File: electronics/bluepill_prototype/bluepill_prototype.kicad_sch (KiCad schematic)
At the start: 8 parts, among them M1 Motor_DC, SW1 SW_SPST, U1 Open_drain_hall_sensor, U2 YAAJ_BluePill_Part_Like

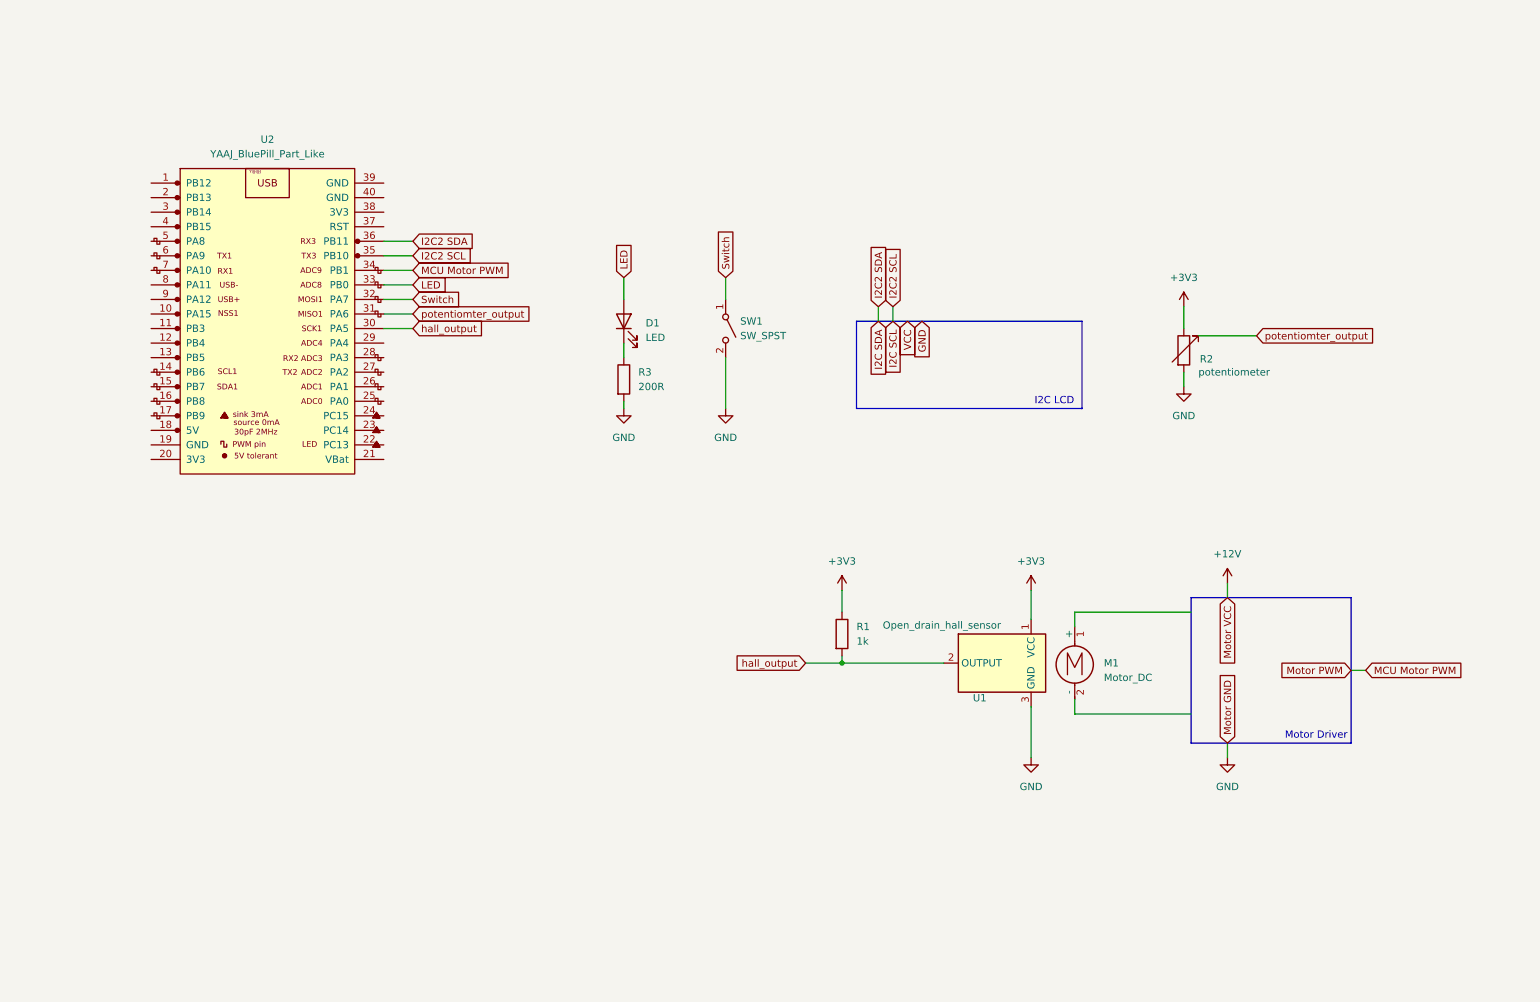
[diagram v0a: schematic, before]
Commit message: feat: updated electronic schematic
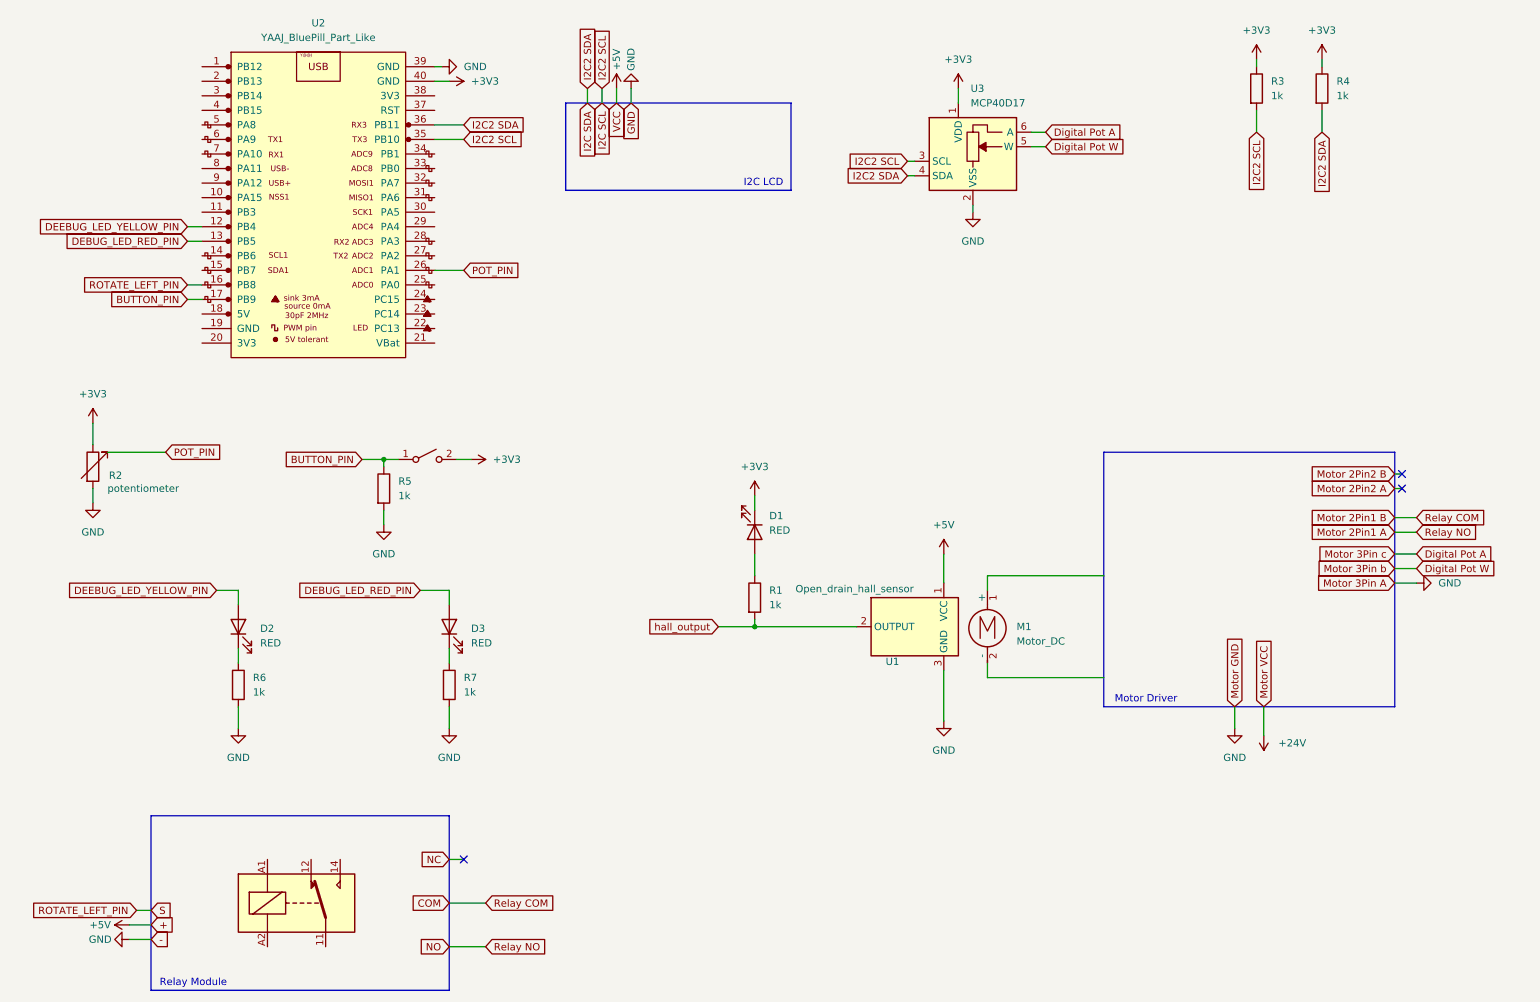
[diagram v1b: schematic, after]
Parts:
- added D2, D3: RED, symbol Device:LED
- added K1: Fujitsu_FTR-LYCA005x, Relay_THT:Relay_SPDT_Fujitsu_FTR-LYCA005x_FormC_Vertical, symbol Relay:Fujitsu_FTR-LYCA005x
- added R4, R5, R6, R7: 1k, symbol Device:R
- added U3: MCP40D17, Package_TO_SOT_SMD:SOT-363_SC-70-6, symbol Potentiometer_Digital:MCP4018-xxxxLT
- D1: value LED -> RED
- R3: value 200R -> 1k
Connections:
- net +3V3: now also D1.1 (K), R3.1, SW1.2 (B), U2.40 (GND), R4.1, U3.1 (VDD); no longer R1.1, U1.1 (VCC)
- net GND: now also U2.39 (GND), R5.2, R6.2, R7.2, U3.2 (VSS); no longer R3.2, SW1.2 (B)
- net I2C SCL: now also R3.2, U3.3 (SCL)
- net I2C SDA: now also R4.2, U3.4 (SDA)
- net hall_output: no longer U2.30 (PA5)
- net DEEBUG_LED_YELLOW_PIN: now reaches U2.12 (PB4)
- net DEEBUG_LED_YELLOW_PIN: now also D2.2 (A)
- net DEBUG_LED_RED_PIN: now reaches U2.13 (PB5)
- net DEBUG_LED_RED_PIN: now also D3.2 (A)
- net ROTATE_LEFT_PIN: now reaches U2.16 (PB8)
- net BUTTON_PIN: now reaches U2.17 (PB9)
- net BUTTON_PIN: now also SW1.1 (A), R5.1
- net POT_PIN: now reaches U2.26 (PA1)
- net LED: no longer names the net of D1.2 (A)
- net LED: now also R1.1; no longer U2.33 (PB0)
- net MCU Motor PWM: no longer names the net of U2.34 (PB1)
- net Switch: no longer names the net of U2.32 (PA7)
- net Switch: no longer SW1.1 (A)
- net potentiomter_output: no longer names the net of U2.31 (PA6)
- new net: D3.1 (K), R7.1
- new net: D2.1 (K), R6.1
- new net +5V: U1.1 (VCC)
- new net Digital Pot A: U3.6 (A)
- new net Digital Pot W: U3.5 (W)
- no-connect marks 0 -> 3
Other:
- note added: "Relay Module"
- moved on the sheet: M1, R1, R2, U1, U2

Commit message: fixed schematic
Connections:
- net I2C SCL: now also U2.14 (PB6); no longer U2.35 (PB10)
- net I2C SDA: now also U2.15 (PB7); no longer U2.36 (PB11)

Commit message: feat: updated prototype schematic
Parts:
- D2: value RED -> Yellow
- D3: value RED -> Red
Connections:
- net POT_PIN: now also U2.29 (PA4); no longer U2.26 (PA1)
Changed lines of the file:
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@@
 	(wire
 		(pts
-			(xy 90.17 68.58) (xy 85.09 68.58)
-		)
-		(stroke
-			(width 0)
-			(type default)
-		)
-	)
-	(wire
-		(pts
 			(xy 111.76 36.83) (xy 111.76 39.37)
 		)
@@
 	(wire
 		(pts
+			(xy 90.17 60.96) (xy 85.09 60.96)
+		)
+		(stroke
+			(width 0)
+			(type default)
+		)
+	)
+	(wire
+		(pts
 			(xy 176.53 36.83) (xy 176.53 39.37)
 		)
@@
 		)
 	)
+	(global_label "POT_PIN"
+		(shape input)
+		(at 90.17 60.96 0)
+		(fields_autoplaced yes)
+		(effects
+			(font
+				(size 1.27 1.27)
+			)
+			(justify left)
+		)
+		(property "Intersheetrefs" "${INTERSHEET_REFS}"
+			(at 100.8962 60.96 0)
+			(effects
+				(font
+					(size 1.27 1.27)
+				)
+				(justify left)
+				(hide yes)
+			)
+		)
+	)
 	(global_label "BUTTON_PIN"
 		(shape input)
@@
 		)
 	)
-	(global_label "POT_PIN"
-		(shape input)
-		(at 90.17 68.58 0)
-		(fields_autoplaced yes)
-		(effects
-			(font
-				(size 1.27 1.27)
-			)
-			(justify left)
-		)
-		(property "Intersheetrefs" "${INTERSHEET_REFS}"
-			(at 100.8962 68.58 0)
-			(effects
-				(font
-					(size 1.27 1.27)
-				)
-				(justify left)
-				(hide yes)
-			)
-		)
-	)
 	(global_label "Motor 2Pin2 B"
 		(shape input)
@@
 			)
 		)
-		(property "Value" "RED"
+		(property "Value" "Yellow"
 			(at 54.61 133.6674 90)
 			(effects
@@
 			)
 		)
-		(property "Value" "RED"
+		(property "Value" "Red"
 			(at 91.44 133.6674 90)
 			(effects

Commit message: added primitive enclosure
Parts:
- removed D1: RED, symbol Device:LED
- removed D2: Yellow, symbol Device:LED
- removed D3: Red, symbol Device:LED
- removed K1: Fujitsu_FTR-LYCA005x, Relay_THT:Relay_SPDT_Fujitsu_FTR-LYCA005x_FormC_Vertical, symbol Relay:Fujitsu_FTR-LYCA005x
- removed M1: Motor_DC, symbol Motor:Motor_DC
- removed R1, R3, R4, R5, R6, R7: 1k, symbol Device:R
- removed R2: potentiometer, symbol Device:R_Variable
- removed U1: Open_drain_hall_sensor, symbol Sensor_Magnetic:SM351LT
- removed U3: MCP40D17, Package_TO_SOT_SMD:SOT-363_SC-70-6, symbol Potentiometer_Digital:MCP4018-xxxxLT
- added J1, J2, J3, J4: Conn_01x05_Pin, symbol Connector:Conn_01x05_Pin
- added RV1: Potentiometer, symbol Device:R_Potentiometer
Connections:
- net +3V3: now also SW1.1 (A), RV1.3; no longer SW1.2 (B)
- net +5V: now also J2.4 (Pin_4), J4.4 (Pin_4)
- net GND: now also J1.5 (Pin_5), J2.5 (Pin_5), J3.5 (Pin_5), J4.5 (Pin_5), RV1.1
- net Hall U: now reaches U2.11 (PB3)
- net Hall U: now also J2.1 (Pin_1), J4.1 (Pin_1)
- net Button pin: now reaches U2.30 (PA5)
- net Button pin: now also SW1.2 (B)
- net Driver EN: now reaches U2.4 (PB15)
- net Driver EN: now also J1.1 (Pin_1), J3.1 (Pin_1)
- net Driver IN3: now reaches U2.5 (PA8)
- net Driver IN3: now also J1.2 (Pin_2), J3.2 (Pin_2)
- net Driver IN2: now reaches U2.6 (PA9)
- net Driver IN2: now also J1.3 (Pin_3), J3.3 (Pin_3)
- net Driver IN1: now reaches U2.7 (PA10)
- net Driver IN1: now also J1.4 (Pin_4), J3.4 (Pin_4)
- net BUTTON_PIN renamed Led Red
- net Led Red: no longer SW1.1 (A)
- net DEBUG_LED_RED_PIN renamed Hall W
- net Hall W: now also J2.3 (Pin_3), J4.3 (Pin_3)
- net DEEBUG_LED_YELLOW_PIN renamed Hall V
- net Hall V: now also J2.2 (Pin_2), J4.2 (Pin_2)
- net POT_PIN renamed Pot pin
- net Pot pin: now also RV1.2
- net ROTATE_LEFT_PIN renamed Led Yellow
- no-connect marks 3 -> 0
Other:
- note added: "Blue Red White Red Black From goldpin header"
- note added: "Interboard connector"
- note removed: "Motor Driver"
- note removed: "Relay Module"
- moved on the sheet: U2
